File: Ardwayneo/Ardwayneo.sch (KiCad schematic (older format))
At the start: 0 parts

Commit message: Add all schematic symbols
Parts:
- added BT?: Battery, symbol Device:Battery
- added C? (x2): C, symbol Device:C
- added C?: CP, symbol Device:CP
- added D?: LED, symbol Device:LED
- added R? (x2): R, symbol Device:R
- added U?: 24LC1025, symbol Memory_EEPROM:24LC1025
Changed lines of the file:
@@
 $Descr A4 11693 8268
 encoding utf-8
-Sheet 1 1
+Sheet 1 2
 Title "Ardwayneo "
 Date "2021-01-02"
@@
 Comment4 ""
 $EndDescr
+$Comp
+L Device:Battery BT?
+U 1 1 5FF1330E
+P 1600 1400
+F 0 "BT?" H 1708 1446 50  0000 L CNN
+F 1 "Battery" H 1708 1355 50  0000 L CNN
+F 2 "" V 1600 1460 50  0001 C CNN
+F 3 "~" V 1600 1460 50  0001 C CNN
+	1    1600 1400
+	1    0    0    -1
+$EndComp
+$Comp
+L Device:C C?
+U 1 1 5FF14682
+P 2300 1350
+F 0 "C?" H 2415 1396 50  0000 L CNN
+F 1 "C" H 2415 1305 50  0000 L CNN
+F 2 "" H 2338 1200 50  0001 C CNN
+F 3 "~" H 2300 1350 50  0001 C CNN
+	1    2300 1350
+	1    0    0    -1
+$EndComp
+$Comp
+L Device:C C?
+U 1 1 5FF15CF4
+P 2300 1775
+F 0 "C?" H 2415 1821 50  0000 L CNN
+F 1 "C" H 2415 1730 50  0000 L CNN
+F 2 "" H 2338 1625 50  0001 C CNN
+F 3 "~" H 2300 1775 50  0001 C CNN
+	1    2300 1775
+	1    0    0    -1
+$EndComp
+$Comp
+L Device:CP C?
+U 1 1 5FF162B4
+P 2300 2250
+F 0 "C?" H 2418 2296 50  0000 L CNN
+F 1 "CP" H 2418 2205 50  0000 L CNN
+F 2 "" H 2338 2100 50  0001 C CNN
+F 3 "~" H 2300 2250 50  0001 C CNN
+	1    2300 2250
+	1    0    0    -1
+$EndComp
+$Comp
+L Device:LED D?
+U 1 1 5FF17C37
+P 1625 2225
+F 0 "D?" H 1618 2442 50  0000 C CNN
+F 1 "LED" H 1618 2351 50  0000 C CNN
+F 2 "" H 1625 2225 50  0001 C CNN
+F 3 "~" H 1625 2225 50  0001 C CNN
+	1    1625 2225
+	1    0    0    -1
+$EndComp
+$Comp
+L Device:R R?
+U 1 1 5FF18E03
+P 3050 1350
+F 0 "R?" H 3120 1396 50  0000 L CNN
+F 1 "R" H 3120 1305 50  0000 L CNN
+F 2 "" V 2980 1350 50  0001 C CNN
+F 3 "~" H 3050 1350 50  0001 C CNN
+	1    3050 1350
+	1    0    0    -1
+$EndComp
+$Comp
+L Device:R R?
+U 1 1 5FF1933E
+P 3050 1775
+F 0 "R?" H 3120 1821 50  0000 L CNN
+F 1 "R" H 3120 1730 50  0000 L CNN
+F 2 "" V 2980 1775 50  0001 C CNN
+F 3 "~" H 3050 1775 50  0001 C CNN
+	1    3050 1775
+	1    0    0    -1
+$EndComp
+$Comp
+L Memory_EEPROM:24LC1025 U?
+U 1 1 5FF1A37B
+P 4025 1575
+F 0 "U?" H 4025 2056 50  0000 C CNN
+F 1 "24LC1025" H 4025 1965 50  0000 C CNN
+F 2 "" H 4025 1575 50  0001 C CNN
+F 3 "http://ww1.microchip.com/downloads/en/DeviceDoc/21941B.pdf" H 4025 1575 50  0001 C CNN
+	1    4025 1575
+	1    0    0    -1
+$EndComp
+$Sheet
+S 3250 2175 1750 1825
+U 5FF1D20B
+F0 "Connectors" 50
+F1 "Connectors.sch" 50
+$EndSheet
 $EndSCHEMATC

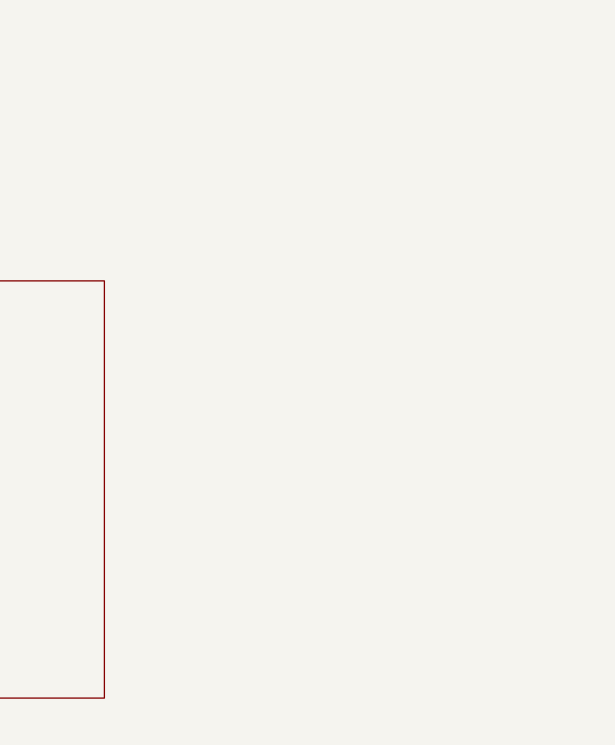
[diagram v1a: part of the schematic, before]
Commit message: Added symbols for connectors and MCU
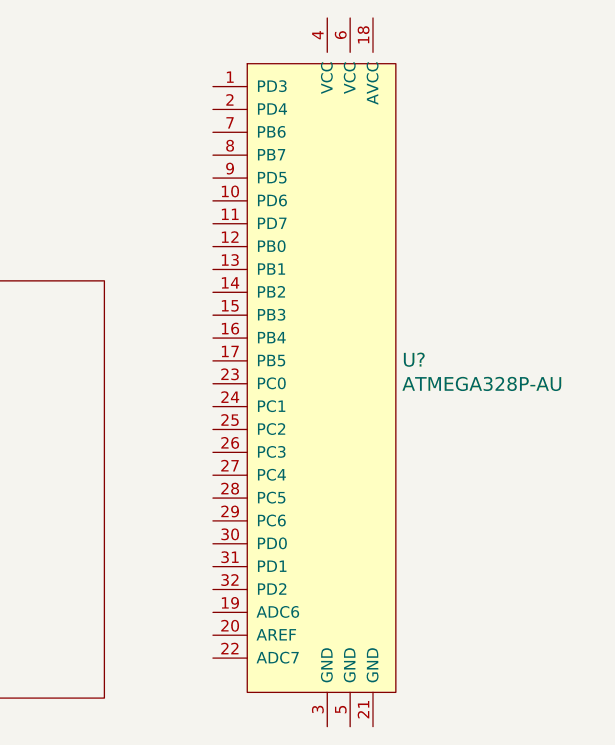
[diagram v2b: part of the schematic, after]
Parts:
- added U?: ATMEGA328P-AU, digikey-footprints:TQFP-32_7x7mm, symbol dk_Embedded-Microcontrollers:ATMEGA328P-AU
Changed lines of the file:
@@
 F1 "Connectors.sch" 50
 $EndSheet
+$Comp
+L dk_Embedded-Microcontrollers:ATMEGA328P-AU U?
+U 1 1 5FF24782
+P 5975 2625
+F 0 "U?" H 6303 2728 60  0000 L CNN
+F 1 "ATMEGA328P-AU" H 6303 2622 60  0000 L CNN
+F 2 "digikey-footprints:TQFP-32_7x7mm" H 6175 2825 60  0001 L CNN
+F 3 "http://www.microchip.com/mymicrochip/filehandler.aspx?ddocname=en608326" H 6175 2925 60  0001 L CNN
+F 4 "ATMEGA328P-AU-ND" H 6175 3025 60  0001 L CNN "Digi-Key_PN"
+F 5 "ATMEGA328P-AU" H 6175 3125 60  0001 L CNN "MPN"
+F 6 "Integrated Circuits (ICs)" H 6175 3225 60  0001 L CNN "Category"
+F 7 "Embedded - Microcontrollers" H 6175 3325 60  0001 L CNN "Family"
+F 8 "http://www.microchip.com/mymicrochip/filehandler.aspx?ddocname=en608326" H 6175 3425 60  0001 L CNN "DK_Datasheet_Link"
+F 9 "/product-detail/en/microchip-technology/ATMEGA328P-AU/ATMEGA328P-AU-ND/1832260" H 6175 3525 60  0001 L CNN "DK_Detail_Page"
+F 10 "IC MCU 8BIT 32KB FLASH 32TQFP" H 6175 3625 60  0001 L CNN "Description"
+F 11 "Microchip Technology" H 6175 3725 60  0001 L CNN "Manufacturer"
+F 12 "Active" H 6175 3825 60  0001 L CNN "Status"
+	1    5975 2625
+	1    0    0    -1
+$EndComp
 $EndSCHEMATC

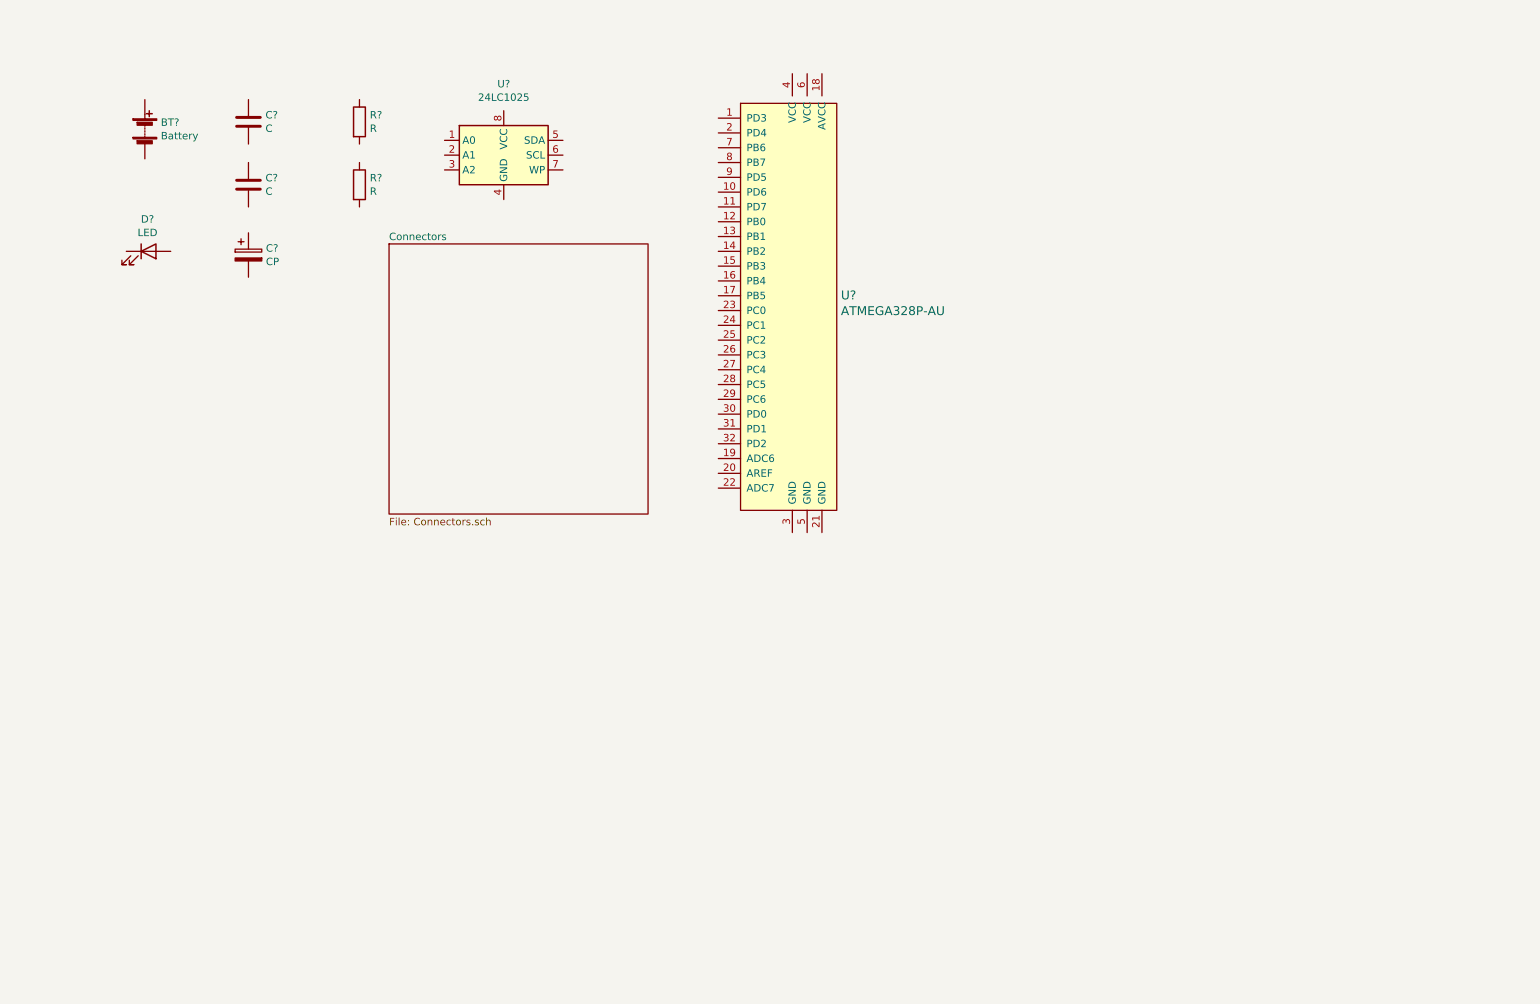
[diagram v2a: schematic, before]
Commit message: Add custom symbol
Added custom symbol for clock IC
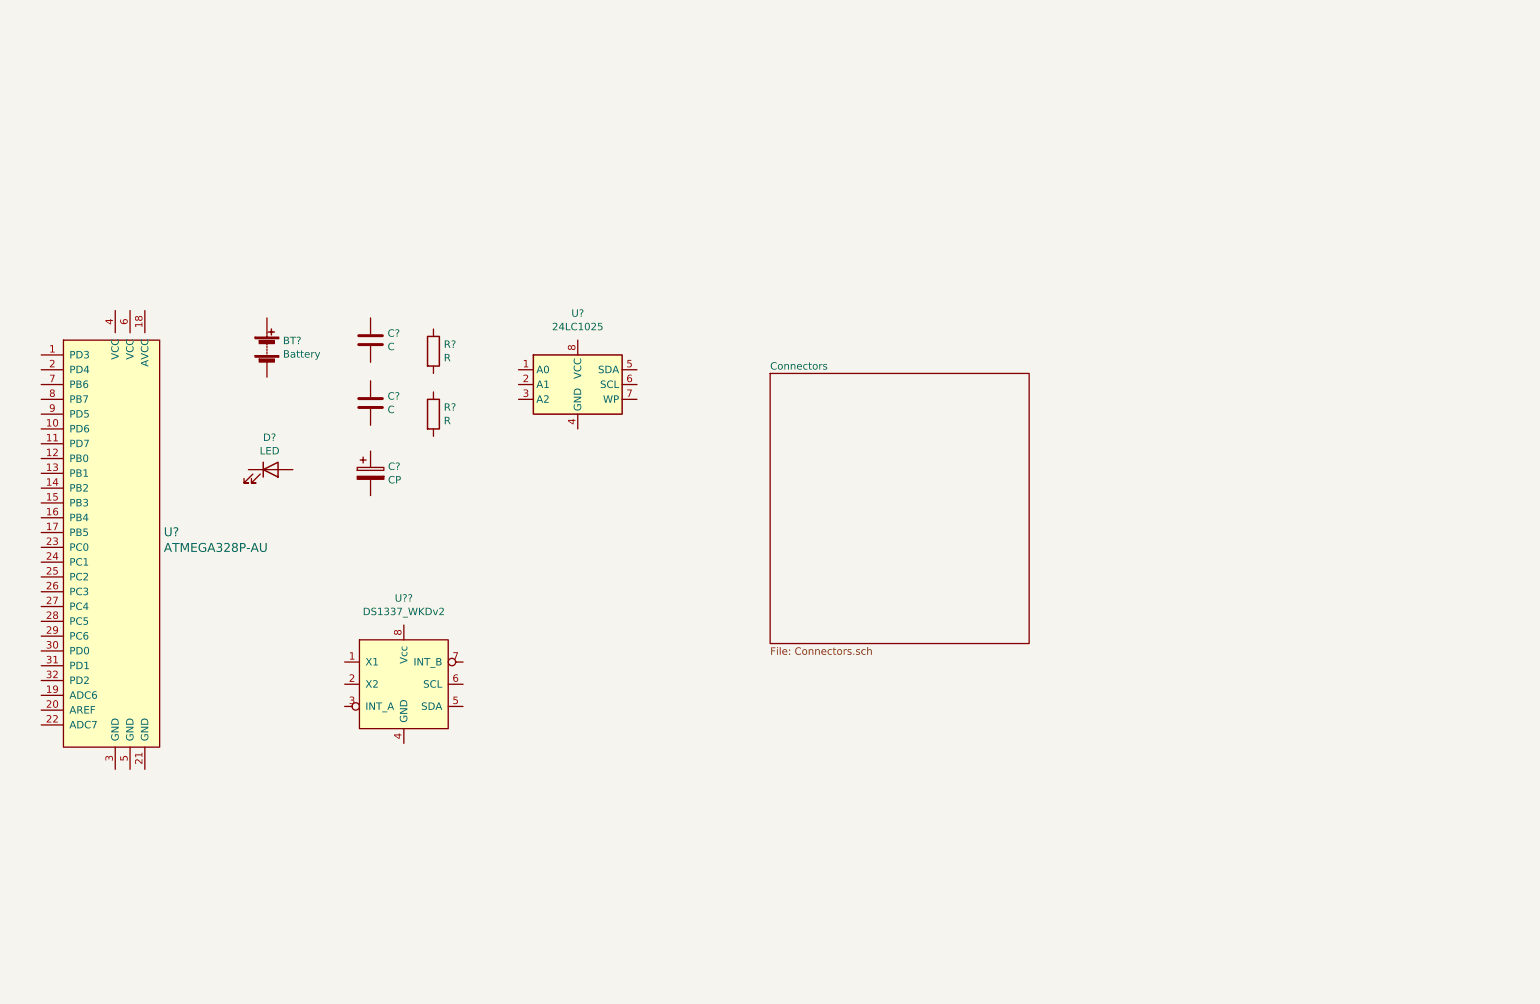
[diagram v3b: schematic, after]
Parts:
- added U??: DS1337_WKDv2, symbol Ardwayneo_Library:DS1337_WKDv2
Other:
- moved on the sheet: BT?, C?, D?, R?, U?
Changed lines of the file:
@@
 L Device:Battery BT?
 U 1 1 5FF1330E
-P 1600 1400
-F 0 "BT?" H 1708 1446 50  0000 L CNN
-F 1 "Battery" H 1708 1355 50  0000 L CNN
-F 2 "" V 1600 1460 50  0001 C CNN
-F 3 "~" V 1600 1460 50  0001 C CNN
-	1    1600 1400
+P 2425 2875
+F 0 "BT?" H 2533 2921 50  0000 L CNN
+F 1 "Battery" H 2533 2830 50  0000 L CNN
+F 2 "" V 2425 2935 50  0001 C CNN
+F 3 "~" V 2425 2935 50  0001 C CNN
+	1    2425 2875
 	1    0    0    -1
 $EndComp
@@
 L Device:C C?
 U 1 1 5FF14682
-P 2300 1350
-F 0 "C?" H 2415 1396 50  0000 L CNN
-F 1 "C" H 2415 1305 50  0000 L CNN
-F 2 "" H 2338 1200 50  0001 C CNN
-F 3 "~" H 2300 1350 50  0001 C CNN
-	1    2300 1350
+P 3125 2825
+F 0 "C?" H 3240 2871 50  0000 L CNN
+F 1 "C" H 3240 2780 50  0000 L CNN
+F 2 "" H 3163 2675 50  0001 C CNN
+F 3 "~" H 3125 2825 50  0001 C CNN
+	1    3125 2825
 	1    0    0    -1
 $EndComp
@@
 L Device:C C?
 U 1 1 5FF15CF4
-P 2300 1775
-F 0 "C?" H 2415 1821 50  0000 L CNN
-F 1 "C" H 2415 1730 50  0000 L CNN
-F 2 "" H 2338 1625 50  0001 C CNN
-F 3 "~" H 2300 1775 50  0001 C CNN
-	1    2300 1775
+P 3125 3250
+F 0 "C?" H 3240 3296 50  0000 L CNN
+F 1 "C" H 3240 3205 50  0000 L CNN
+F 2 "" H 3163 3100 50  0001 C CNN
+F 3 "~" H 3125 3250 50  0001 C CNN
+	1    3125 3250
 	1    0    0    -1
 $EndComp
@@
 L Device:CP C?
 U 1 1 5FF162B4
-P 2300 2250
-F 0 "C?" H 2418 2296 50  0000 L CNN
-F 1 "CP" H 2418 2205 50  0000 L CNN
-F 2 "" H 2338 2100 50  0001 C CNN
-F 3 "~" H 2300 2250 50  0001 C CNN
-	1    2300 2250
+P 3125 3725
+F 0 "C?" H 3243 3771 50  0000 L CNN
+F 1 "CP" H 3243 3680 50  0000 L CNN
+F 2 "" H 3163 3575 50  0001 C CNN
+F 3 "~" H 3125 3725 50  0001 C CNN
+	1    3125 3725
 	1    0    0    -1
 $EndComp
@@
 L Device:LED D?
 U 1 1 5FF17C37
-P 1625 2225
-F 0 "D?" H 1618 2442 50  0000 C CNN
-F 1 "LED" H 1618 2351 50  0000 C CNN
-F 2 "" H 1625 2225 50  0001 C CNN
-F 3 "~" H 1625 2225 50  0001 C CNN
-	1    1625 2225
+P 2450 3700
+F 0 "D?" H 2443 3917 50  0000 C CNN
+F 1 "LED" H 2443 3826 50  0000 C CNN
+F 2 "" H 2450 3700 50  0001 C CNN
+F 3 "~" H 2450 3700 50  0001 C CNN
+	1    2450 3700
 	1    0    0    -1
 $EndComp
@@
 L Device:R R?
 U 1 1 5FF18E03
-P 3050 1350
-F 0 "R?" H 3120 1396 50  0000 L CNN
-F 1 "R" H 3120 1305 50  0000 L CNN
-F 2 "" V 2980 1350 50  0001 C CNN
-F 3 "~" H 3050 1350 50  0001 C CNN
-	1    3050 1350
+P 3550 2900
+F 0 "R?" H 3620 2946 50  0000 L CNN
+F 1 "R" H 3620 2855 50  0000 L CNN
+F 2 "" V 3480 2900 50  0001 C CNN
+F 3 "~" H 3550 2900 50  0001 C CNN
+	1    3550 2900
 	1    0    0    -1
 $EndComp
@@
 L Device:R R?
 U 1 1 5FF1933E
-P 3050 1775
-F 0 "R?" H 3120 1821 50  0000 L CNN
-F 1 "R" H 3120 1730 50  0000 L CNN
-F 2 "" V 2980 1775 50  0001 C CNN
-F 3 "~" H 3050 1775 50  0001 C CNN
-	1    3050 1775
+P 3550 3325
+F 0 "R?" H 3620 3371 50  0000 L CNN
+F 1 "R" H 3620 3280 50  0000 L CNN
+F 2 "" V 3480 3325 50  0001 C CNN
+F 3 "~" H 3550 3325 50  0001 C CNN
+	1    3550 3325
 	1    0    0    -1
 $EndComp
@@
 L Memory_EEPROM:24LC1025 U?
 U 1 1 5FF1A37B
-P 4025 1575
-F 0 "U?" H 4025 2056 50  0000 C CNN
-F 1 "24LC1025" H 4025 1965 50  0000 C CNN
-F 2 "" H 4025 1575 50  0001 C CNN
-F 3 "http://ww1.microchip.com/downloads/en/DeviceDoc/21941B.pdf" H 4025 1575 50  0001 C CNN
-	1    4025 1575
+P 4525 3125
+F 0 "U?" H 4525 3606 50  0000 C CNN
+F 1 "24LC1025" H 4525 3515 50  0000 C CNN
+F 2 "" H 4525 3125 50  0001 C CNN
+F 3 "http://ww1.microchip.com/downloads/en/DeviceDoc/21941B.pdf" H 4525 3125 50  0001 C CNN
+	1    4525 3125
 	1    0    0    -1
 $EndComp
 $Sheet
-S 3250 2175 1750 1825
+S 5825 3050 1750 1825
 U 5FF1D20B
 F0 "Connectors" 50
@@
 L dk_Embedded-Microcontrollers:ATMEGA328P-AU U?
 U 1 1 5FF24782
-P 5975 2625
-F 0 "U?" H 6303 2728 60  0000 L CNN
-F 1 "ATMEGA328P-AU" H 6303 2622 60  0000 L CNN
-F 2 "digikey-footprints:TQFP-32_7x7mm" H 6175 2825 60  0001 L CNN
-F 3 "http://www.microchip.com/mymicrochip/filehandler.aspx?ddocname=en608326" H 6175 2925 60  0001 L CNN
-F 4 "ATMEGA328P-AU-ND" H 6175 3025 60  0001 L CNN "Digi-Key_PN"
-F 5 "ATMEGA328P-AU" H 6175 3125 60  0001 L CNN "MPN"
-F 6 "Integrated Circuits (ICs)" H 6175 3225 60  0001 L CNN "Category"
-F 7 "Embedded - Microcontrollers" H 6175 3325 60  0001 L CNN "Family"
-F 8 "http://www.microchip.com/mymicrochip/filehandler.aspx?ddocname=en608326" H 6175 3425 60  0001 L CNN "DK_Datasheet_Link"
-F 9 "/product-detail/en/microchip-technology/ATMEGA328P-AU/ATMEGA328P-AU-ND/1832260" H 6175 3525 60  0001 L CNN "DK_Detail_Page"
-F 10 "IC MCU 8BIT 32KB FLASH 32TQFP" H 6175 3625 60  0001 L CNN "Description"
-F 11 "Microchip Technology" H 6175 3725 60  0001 L CNN "Manufacturer"
-F 12 "Active" H 6175 3825 60  0001 L CNN "Status"
-	1    5975 2625
+P 1400 4225
+F 0 "U?" H 1728 4328 60  0000 L CNN
+F 1 "ATMEGA328P-AU" H 1728 4222 60  0000 L CNN
+F 2 "digikey-footprints:TQFP-32_7x7mm" H 1600 4425 60  0001 L CNN
+F 3 "http://www.microchip.com/mymicrochip/filehandler.aspx?ddocname=en608326" H 1600 4525 60  0001 L CNN
+F 4 "ATMEGA328P-AU-ND" H 1600 4625 60  0001 L CNN "Digi-Key_PN"
+F 5 "ATMEGA328P-AU" H 1600 4725 60  0001 L CNN "MPN"
+F 6 "Integrated Circuits (ICs)" H 1600 4825 60  0001 L CNN "Category"
+F 7 "Embedded - Microcontrollers" H 1600 4925 60  0001 L CNN "Family"
+F 8 "http://www.microchip.com/mymicrochip/filehandler.aspx?ddocname=en608326" H 1600 5025 60  0001 L CNN "DK_Datasheet_Link"
+F 9 "/product-detail/en/microchip-technology/ATMEGA328P-AU/ATMEGA328P-AU-ND/1832260" H 1600 5125 60  0001 L CNN "DK_Detail_Page"
+F 10 "IC MCU 8BIT 32KB FLASH 32TQFP" H 1600 5225 60  0001 L CNN "Description"
+F 11 "Microchip Technology" H 1600 5325 60  0001 L CNN "Manufacturer"
+F 12 "Active" H 1600 5425 60  0001 L CNN "Status"
+	1    1400 4225
 	1    0    0    -1
 $EndComp
+$Comp
+L Ardwayneo_Library:DS1337_WKDv2 U??
+U 1 1 5FF2FA48
+P 3350 5150
+F 0 "U??" H 3350 5731 50  0000 C CNN
+F 1 "DS1337_WKDv2" H 3350 5640 50  0000 C CNN
+F 2 "" H 3350 5150 50  0001 C CNN
+F 3 "https://datasheets.maximintegrated.com/en/ds/DS1337-DS1337C.pdf" H 3350 5150 50  0001 C CNN
+	1    3350 5150
+	1    0    0    -1
+$EndComp
